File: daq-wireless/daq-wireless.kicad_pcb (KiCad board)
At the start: 2 copper layers, 85 x 85 mm, 41 parts, among them J1 5223004-2, J2 Micro_SD_Card, J3 USB_C_Receptacle_USB2.0, Q1 MMBT3904, Q2 MMBT3904, SW1 RESET, U1 ESP32-WROOM-32, U2 AMS1117, U3 FT231XS, U4 Ebyte_E01-ML01SP4

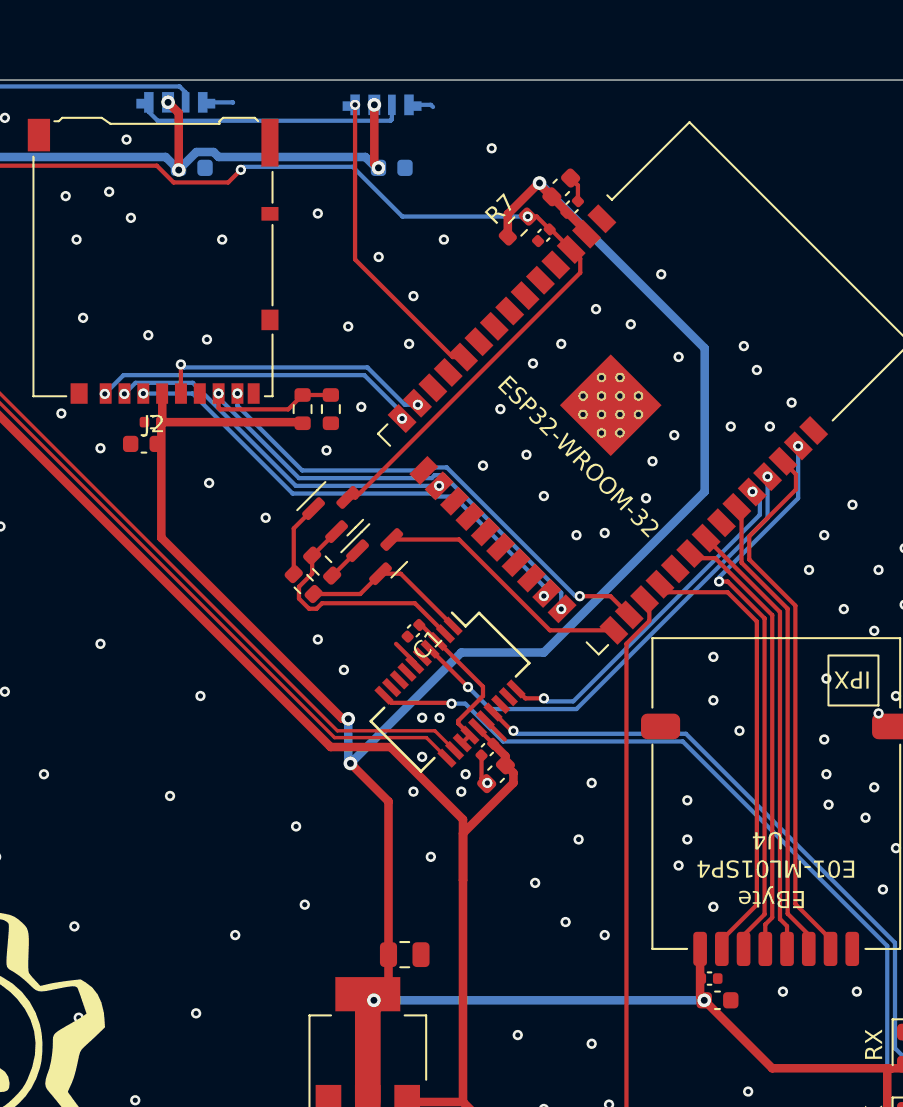
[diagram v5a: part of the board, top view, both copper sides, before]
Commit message: Change CE pin away from UART tx
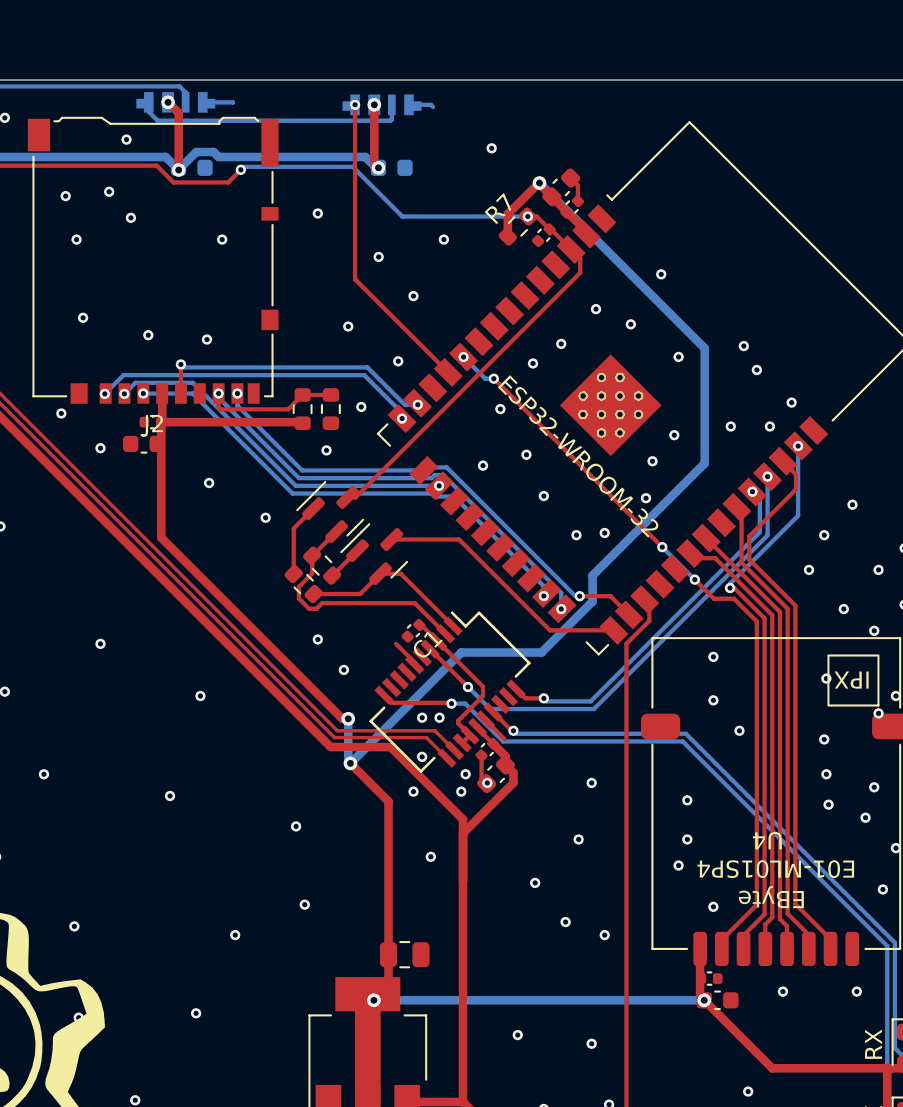
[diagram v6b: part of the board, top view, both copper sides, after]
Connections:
- U1 pad 10: /ARGB -> /RADIO_CE
- U1 pad 11: unconnected-(U1-IO26-Pad11) -> /ARGB
- U1 pad 28: /RADIO_CE -> unconnected-(U1-IO17-Pad28)
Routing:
- net /RADIO_CE: track 26.0 -> 43.0 mm, vias 0 -> 4
- net /RADIO_CS: track 33.2 -> 31.7 mm
- net +3V3: track 154.2 -> 152.8 mm
- net /TXD: track 20.6 -> 21.2 mm
- net /RXD: track 28.2 -> 28.8 mm

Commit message: BOM
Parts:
- C10: footprint Capacitor_SMD:C_0402_1005Metric -> Capacitor_SMD:C_0603_1608Metric
- moved C10 0.57 mm to (152.4, 55.4)
- moved R7 0.57 mm to (150.9, 54.4)

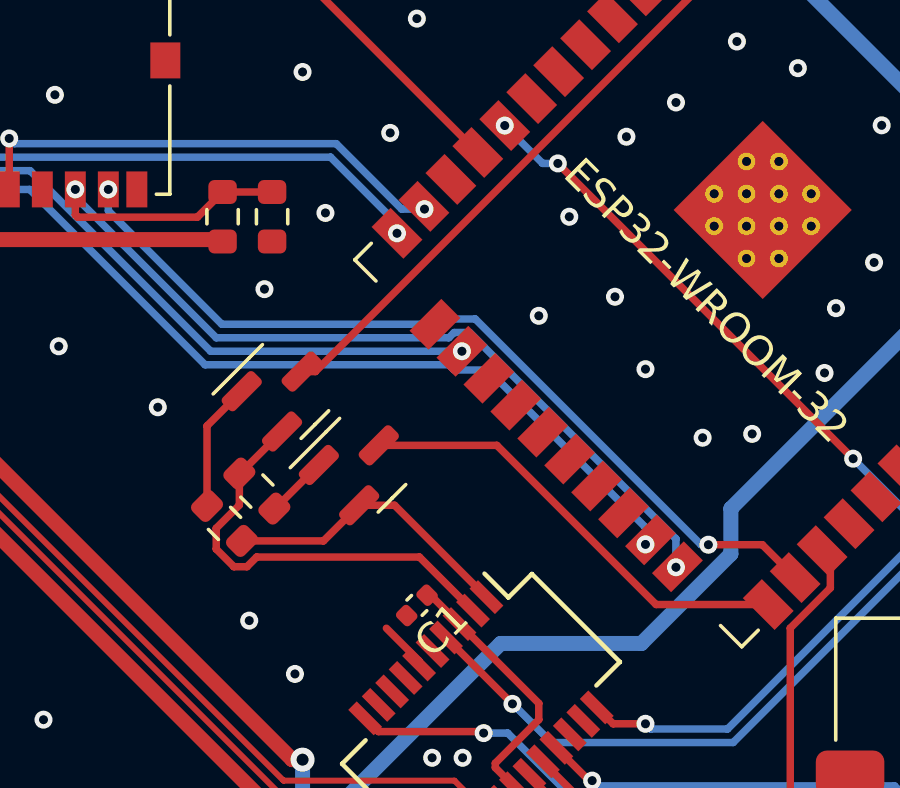
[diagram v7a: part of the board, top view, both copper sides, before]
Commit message: Bugfix DAQ board
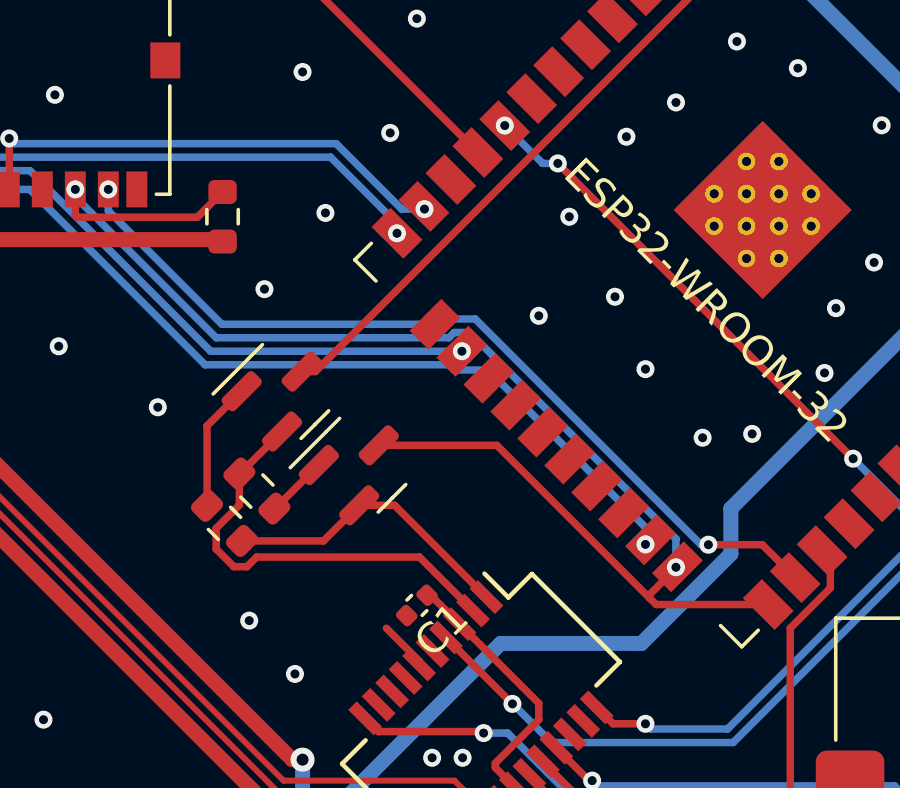
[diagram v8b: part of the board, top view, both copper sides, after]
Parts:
- removed R9: 10k, Resistor_SMD:R_0603_1608Metric
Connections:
- J2 pad 7: /SD0 -> /IO0
- R8 pad 2: /SD0 -> /IO0
- U1 pad 24: /SD0 -> /IO0
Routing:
- net /SD0: track 33.9 -> 0.00 mm, vias 2 -> 0
- net /IO0: track 15.2 -> 48.8 mm, vias 0 -> 2
